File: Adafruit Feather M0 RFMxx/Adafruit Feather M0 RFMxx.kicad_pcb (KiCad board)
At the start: 2 copper layers, 50.8 x 22.9 mm, 41 parts, among them SW1 SPST_TACT-KMR2, U1 2MB Flash, U2 AP2112K-3.3, U3 MCP73831T-2ACI/OT, U4 RFM69HCW, X1 JSTPH, X2 32.768, X3 microUSB, X4 uFL

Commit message: This is version 0.1 of qwiic and flash board.
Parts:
- added U$31: MOUNTINGHOLE2.5, Adafruit Feather M0 RFMxx:MOUNTINGHOLE_2.5_PLATED, F.Cu at (141.6, 119.2)
- added U$31: MOUNTINGHOLE2.5, Adafruit Feather M0 RFMxx:MOUNTINGHOLE_2.5_PLATED, F.Cu at (171.4, 96.1)
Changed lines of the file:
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@@
     (tracks 871)
     (zones 0)
-    (modules 41)
+    (modules 43)
     (nets 58)
   )
   (page A4)
   (layers
-    (0 Top signal hide)
-    (31 Bottom signal)
+    (0 Top signal)
+    (31 Bottom signal hide)
     (32 B.Adhes user hide)
     (33 F.Adhes user hide)
     (34 B.Paste user hide)
     (35 F.Paste user hide)
-    (36 B.SilkS user)
+    (36 B.SilkS user hide)
     (37 F.SilkS user hide)
     (38 B.Mask user hide)
     (39 F.Mask user hide)
-    (40 Dwgs.User user)
+    (40 Dwgs.User user hide)
     (41 Cmts.User user hide)
     (42 Eco1.User user hide)
@@
     (mod_text_size 1 1)
     (mod_text_width 0.15)
-    (pad_size 1.524 1.524)
-    (pad_drill 0.762)
+    (pad_size 2.5 2.5)
+    (pad_drill 2.5)
     (pad_to_mask_clearance 0.051)
     (solder_mask_min_width 0.25)
@@
     (add_net VBUS)
   )
+  (module "Adafruit Feather M0 RFMxx:MOUNTINGHOLE_2.5_PLATED" (layer Top)
+    (at 141.6431 119.2276 270)
+    (fp_text reference U$31 (at 0 0 270) (layer F.SilkS) hide
+      (effects (font (size 1.27 1.27) (thickness 0.15)) (justify right top))
+    )
+    (fp_text value MOUNTINGHOLE2.5 (at 0 0 270) (layer F.SilkS) hide
+      (effects (font (size 1.27 1.27) (thickness 0.15)) (justify right top))
+    )
+    (fp_circle (center 0 0) (end 2 0) (layer F.SilkS) (width 0.2032))
+    (fp_circle (center 0 0) (end 1 0) (layer Dwgs.User) (width 2.032))
+    (fp_circle (center 0 0) (end 1 0) (layer Dwgs.User) (width 2.032))
+    (fp_circle (center 0 0) (end 1 0) (layer Dwgs.User) (width 2.032))
+    (fp_circle (center 0 0) (end 1 0) (layer Dwgs.User) (width 2.032))
+    (pad "" np_thru_hole circle (at -5.334 -29.718 270) (size 2.5 2.5) (drill 2.5) (layers *.Cu *.Mask)
+      (solder_mask_margin 0.0508))
+  )
+  (module "Adafruit Feather M0 RFMxx:MOUNTINGHOLE_2.5_PLATED" (layer Top)
+    (at 171.45 96.139 270)
+    (fp_text reference U$31 (at 0 0 270) (layer F.SilkS) hide
+      (effects (font (size 1.27 1.27) (thickness 0.15)) (justify right top))
+    )
+    (fp_text value MOUNTINGHOLE2.5 (at 0 0 270) (layer F.SilkS) hide
+      (effects (font (size 1.27 1.27) (thickness 0.15)) (justify right top))
+    )
+    (fp_circle (center 0 0) (end 2 0) (layer F.SilkS) (width 0.2032))
+    (fp_circle (center 0 0) (end 1 0) (layer Dwgs.User) (width 2.032))
+    (fp_circle (center 0 0) (end 1 0) (layer Dwgs.User) (width 2.032))
+    (fp_circle (center 0 0) (end 1 0) (layer Dwgs.User) (width 2.032))
+    (fp_circle (center 0 0) (end 1 0) (layer Dwgs.User) (width 2.032))
+    (pad "" np_thru_hole circle (at -0.0254 0.0889 270) (size 2.5 2.5) (drill 2.5) (layers *.Cu *.Mask)
+      (solder_mask_margin 0.0508))
+  )
   (module "Adafruit Feather M0 RFMxx:0805-NO" (layer Top)

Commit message: Parts mostly added. Need to confirm footprints. Before eliminating RFM parts.
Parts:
- added C31: 0.1uF, Adafruit Feather M0 RFMxx:0603-NO, F.Cu at (162.0, 85.8)
- added C32: 0.1uF, Adafruit Feather M0 RFMxx:0603-NO, F.Cu at (162.0, 87.3)
- added C33: 0.1uF, Adafruit Feather M0 RFMxx:0603-NO, F.Cu at (165.0, 85.8)
- added C35, C36: 22pF, Adafruit Feather M0 RFMxx:0603-NO, F.Cu at (148.5, 126.5)
- added J31: Conn_01x02, Socket_Strips:Socket_Strip_Straight_1x02_Pitch2.54mm, F.Cu at (175.8, 82.5)
- added J32: Conn_01x02, Pin_Headers:Pin_Header_Straight_1x02_Pitch2.54mm, F.Cu at (178.7, 88.0)
- added J33: Conn_01x02, Pin_Headers:Pin_Header_Straight_1x02_Pitch2.54mm, F.Cu at (197.7, 90.9)
- added R31: 60, Adafruit Feather M0 RFMxx:0603-NO, F.Cu at (176.7, 102.7)
- added R32: 60, Adafruit Feather M0 RFMxx:0603-NO, F.Cu at (176.7, 108.2)
- added U31: MCP25625-x-SS, Housings_SSOP:SSOP-28_5.3x10.2mm_Pitch0.65mm, F.Cu at (162.0, 106.4)
- added X31: XTAL-3.2X1.5, Adafruit Feather M0 RFMxx:XTAL3215, F.Cu at (185.4, 85.8)
- JP7: footprint SM04B-SRSS-TB(LFSN) -> SM04B-SRSS-TB(LF)(SN):SM04B-SRSS-TB(LFSN)
- moved U4 25.2 mm to (187.4, 104.7)
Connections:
- U4 pad 14P: /TXD_RST -> Net-(U4-Pad14P)
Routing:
- net Net-(U31-Pad20): vias 0 -> 1
- net GND: vias 32 -> 31

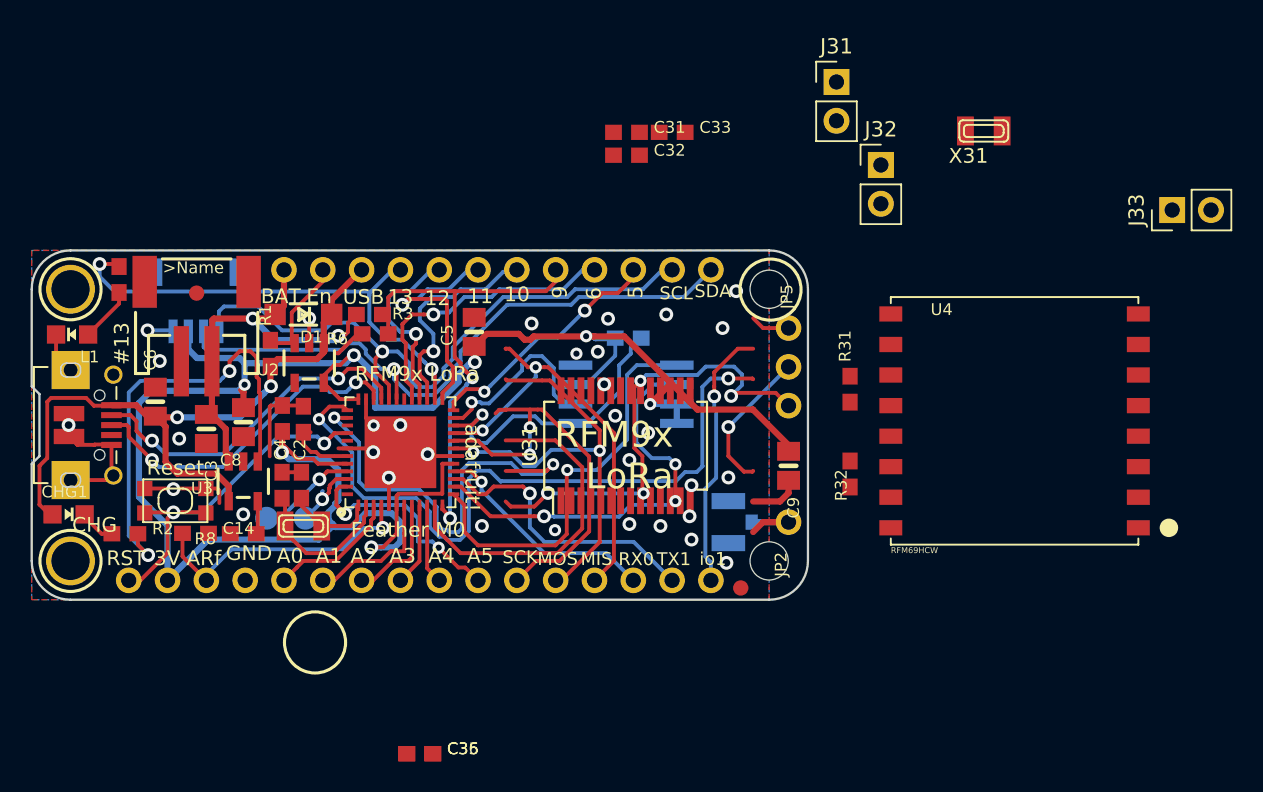
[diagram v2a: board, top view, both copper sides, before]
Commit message: Eliminated RFM and associated parts. Started to place and route. Must still confirm footprints.
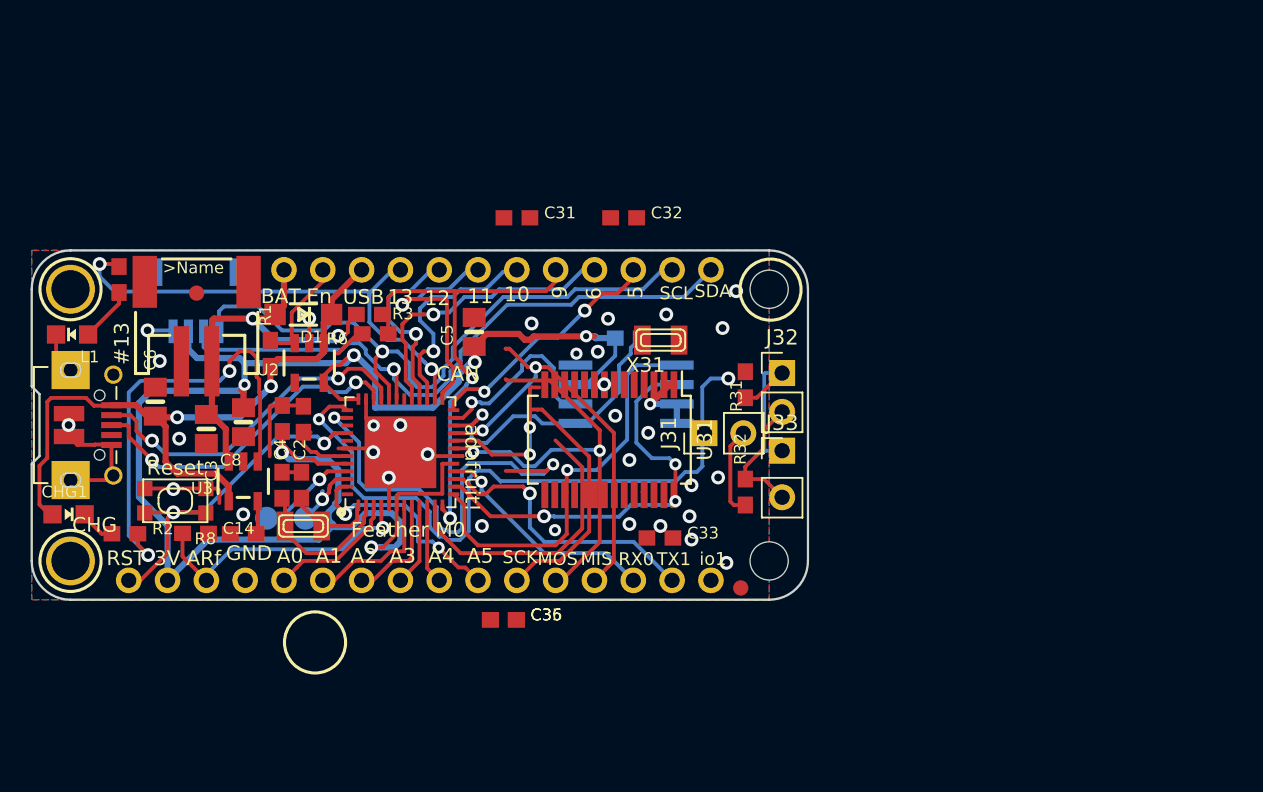
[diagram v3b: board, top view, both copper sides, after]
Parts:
- removed C9: 10uF, Adafruit Feather M0 RFMxx:0805-NO
- removed JP2: HEADER-1X1ROUND, Adafruit Feather M0 RFMxx:1X01_ROUND
- removed JP5: HEADER-1X3ROUND, Adafruit Feather M0 RFMxx:1X03_ROUND
- removed U4: RFM69HCW, Adafruit Feather M0 RFMxx:RFMHCW_SMT
- removed X4: uFL, Adafruit Feather M0 RFMxx:U.FL
- moved J33 30.3 mm to (172.2, 107.2), turned to 0 degrees
- moved C33 26.6 mm to (164.2, 112.4)
- moved X31 25.2 mm to (164.3, 99.4)
- moved J31 24.6 mm to (167.1, 105.5), turned to 90 degrees
- moved J32 15.1 mm to (172.2, 101.6)
- moved C35 10.3 mm to (154.0, 117.7)
- moved C36 10.3 mm to (154.0, 117.7)
- moved C31 9.10 mm to (154.9, 91.4)
- moved R32 6.96 mm to (169.8, 109.4), turned to 90 degrees
- moved R31 6.86 mm to (169.8, 102.4), turned to 270 degrees
- moved C32 4.10 mm to (161.8, 91.4)
- moved U31 1.13 mm to (160.9, 106.0), turned to 270 degrees
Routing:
- net /DIO5: track 30.5 -> 0.00 mm, vias 4 -> 0
- net /DIO1: track 17.3 -> 0.00 mm, vias 1 -> 0
- net +3V3: track 137.8 -> 121.7 mm
- net Net-(J32-Pad1): track 0.00 -> 10.4 mm
- net /DIO3: track 9.54 -> 0.00 mm, vias 1 -> 0
- net Net-(J32-Pad2): track 0.00 -> 8.30 mm
- net Net-(J31-Pad2): track 0.00 -> 5.90 mm
- net Net-(JP2-Pad1): track 5.00 -> 0.00 mm
- net GND: track 50.8 -> 47.1 mm
- net /D8_CS: track 22.2 -> 19.0 mm
- net /DIO2: track 2.58 -> 0.00 mm
- net /RXD_IRQ: track 46.0 -> 44.4 mm
- net Net-(U31-Pad20): vias 1 -> 0
- net Net-(C35-Pad1): vias 0 -> 1
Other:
- board text added: "CAN"
- board text removed: "RFM9x LoRa"

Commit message: Routing ...
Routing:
- net VBUS: track 44.9 -> 67.6 mm, vias 2 -> 3
- net /RXD_IRQ: track 44.4 -> 22.6 mm, vias 2 -> 1
- net /MOSI: track 29.3 -> 20.4 mm
- net /D8_CS: track 19.0 -> 10.2 mm
- net /TXD_RST: track 28.4 -> 25.1 mm
- net /MISO: track 27.1 -> 24.6 mm

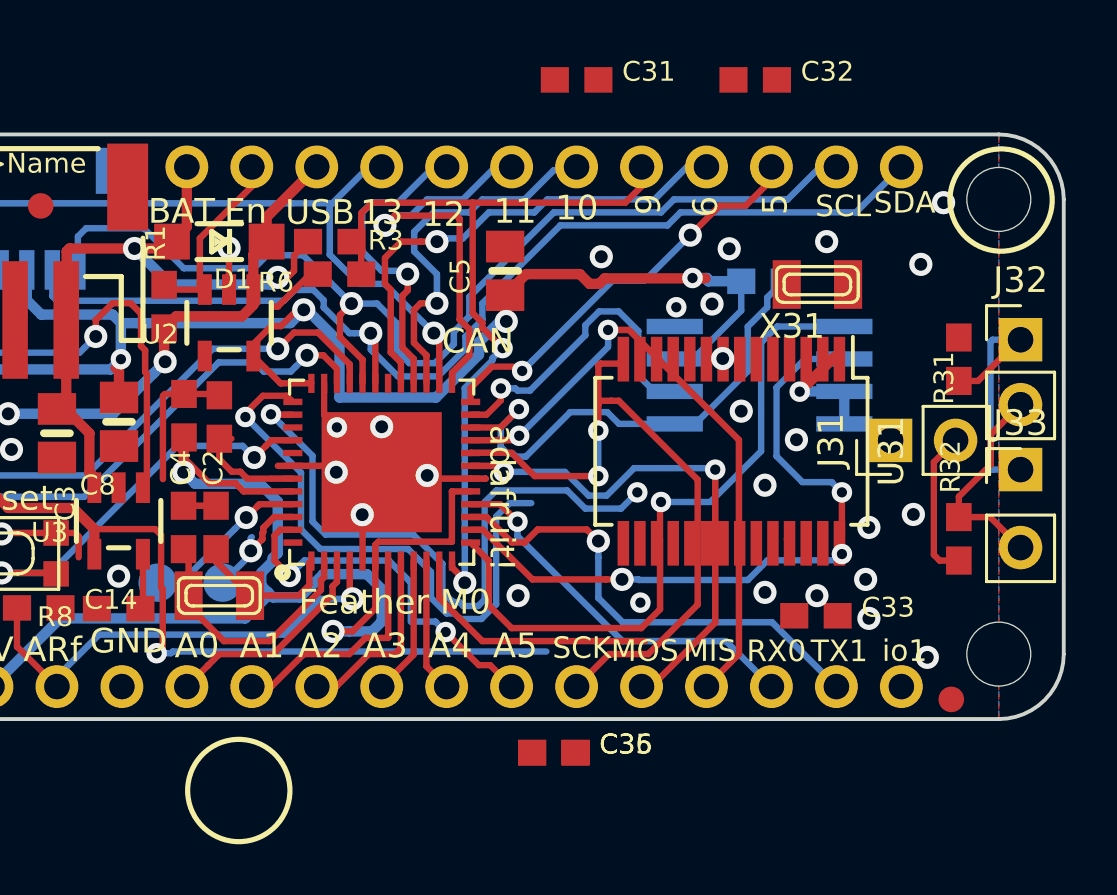
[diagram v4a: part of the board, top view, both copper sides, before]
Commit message: Routed, with some remaining errors: - some grounds disconnected - odd error about runner on PAD25 of MCP too close to PAD24. But there is no runner on PAD25 - just the footprint itself.
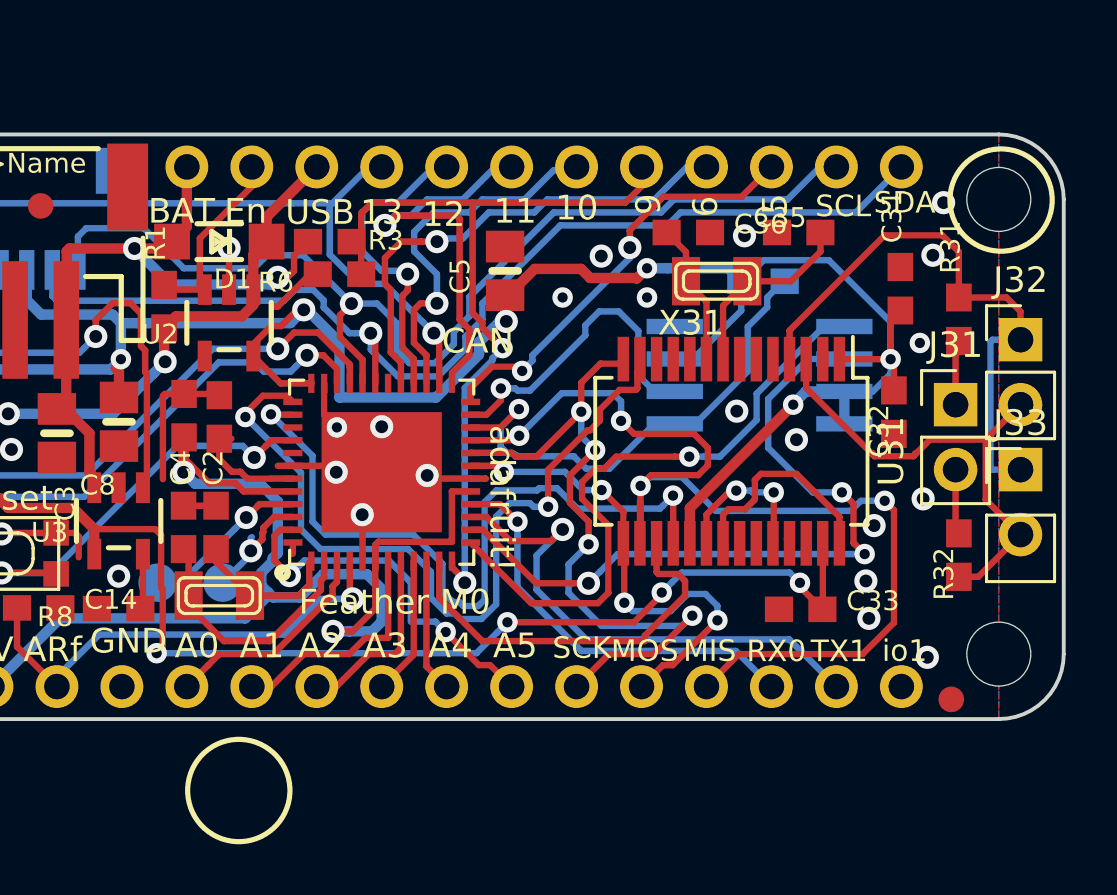
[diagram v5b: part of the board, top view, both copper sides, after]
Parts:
- J31: footprint Socket_Strips:Socket_Strip_Straight_1x02_Pitch2.54mm -> Pin_Headers:Pin_Header_Straight_1x02_Pitch2.54mm
- moved C35 22.5 mm to (163.5, 97.4), turned to 180 degrees
- moved C36 21.0 mm to (159.2, 97.4)
- moved C31 15.1 mm to (167.5, 99.6), turned to 90 degrees
- moved C32 14.1 mm to (167.3, 104.4), turned to 270 degrees
- moved X31 3.94 mm to (160.3, 99.3)
- moved J31 2.90 mm to (169.7, 104.1), turned to 0 degrees
- moved R31 1.56 mm to (169.8, 100.8), turned to 90 degrees
- moved C33 0.65 mm to (163.6, 112.1)
- moved R32 0.64 mm to (169.8, 110.0), turned to 270 degrees
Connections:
- net Net-(U$4-Pad39) renamed /TXLED
- net Net-(U$4-Pad41) renamed /USBHOSTEN
- net Net-(U$4-Pad48) renamed /RXLED
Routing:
- net +3V3: track 121.7 -> 143.6 mm, vias 7 -> 8
- net /MISO: track 24.6 -> 42.6 mm, vias 2 -> 4
- net VBUS: track 67.6 -> 83.2 mm, vias 3 -> 6
- net Net-(J32-Pad1): track 10.4 -> 22.5 mm
- net Net-(J32-Pad2): track 8.30 -> 18.9 mm
- net Net-(U31-Pad21): track 0.00 -> 8.52 mm
- net /RXD_IRQ: track 22.6 -> 31.0 mm, vias 1 -> 2
- net Net-(C35-Pad1): track 0.00 -> 7.53 mm, vias 1 -> 0
- net Net-(U31-Pad20): track 0.00 -> 6.18 mm, vias 0 -> 2
- net Net-(C36-Pad1): track 0.00 -> 5.60 mm
- net /D8_CS: track 10.2 -> 15.6 mm
- net Net-(J31-Pad2): track 5.90 -> 2.54 mm
- net /TXD_RST: track 25.1 -> 28.4 mm
- net /D4_FLASHMOSI: track 27.6 -> 24.7 mm
- net Net-(J31-Pad1): track 0.00 -> 2.54 mm
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
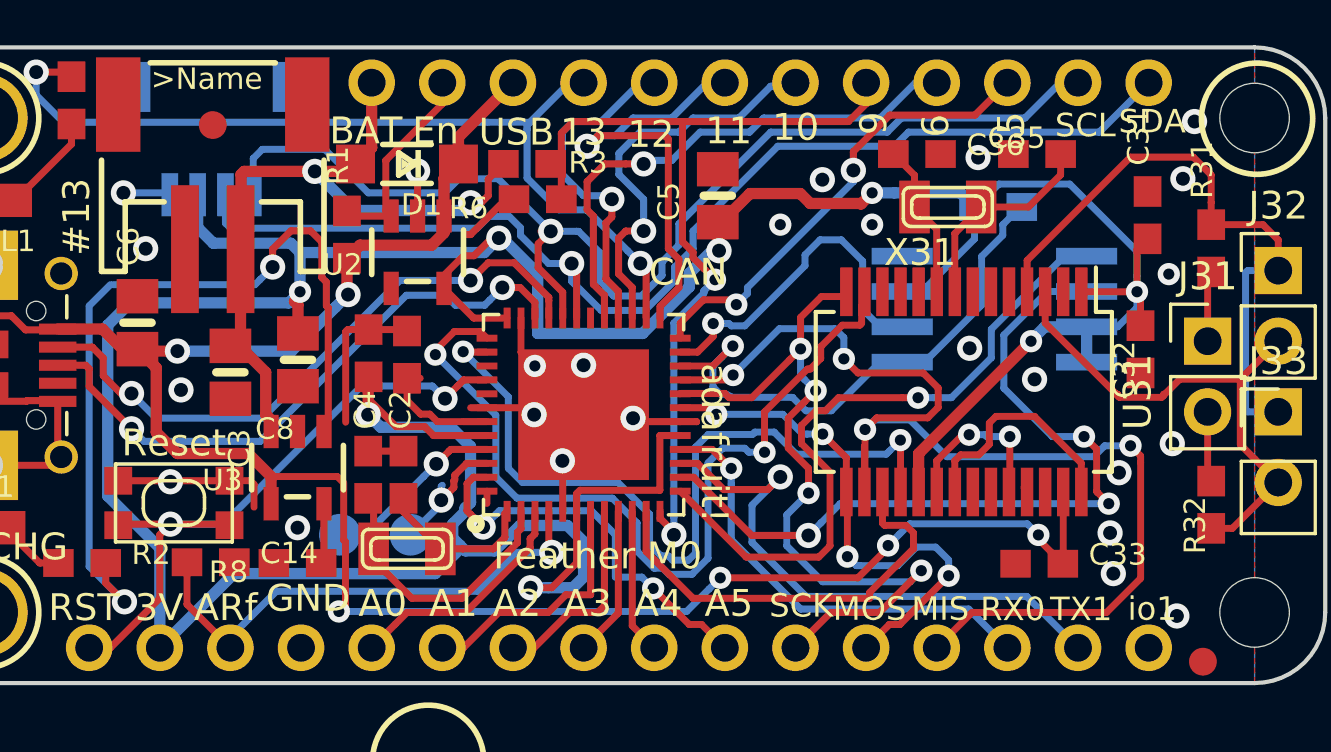
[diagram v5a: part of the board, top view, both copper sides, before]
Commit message: Fixed DRC errors. Remaining are ignores? - 2 pads part of USB connector - Top and Bottom regions not connected
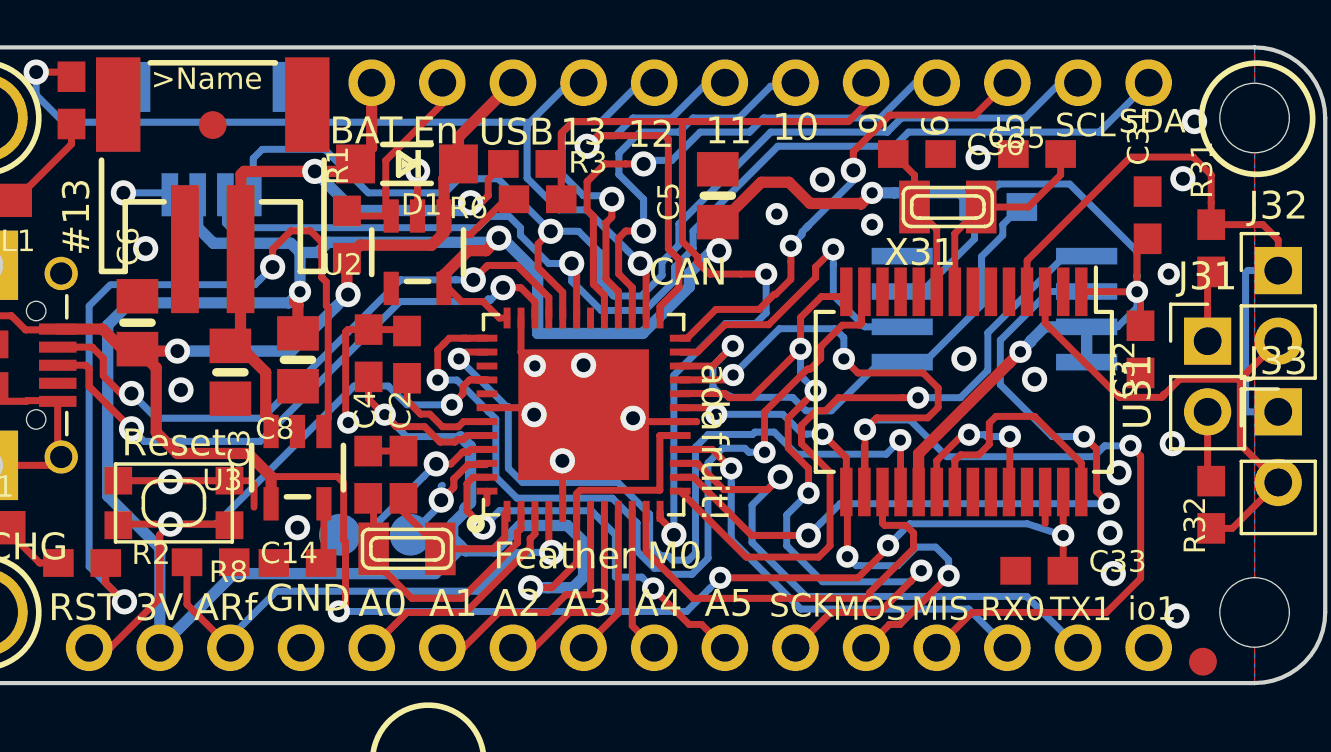
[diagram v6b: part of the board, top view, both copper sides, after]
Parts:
- moved C33 0.25 mm to (163.6, 112.4)
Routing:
- net /D9: track 31.9 -> 35.3 mm
- net +3V3: track 143.6 -> 141.1 mm
- net /~RESET: track 24.2 -> 25.0 mm
- net GND: track 47.1 -> 47.7 mm, vias 26 -> 27

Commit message: On MCP25625, added connection from STBY to GND to put device in Normal mode.
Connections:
- U31 pad 5: Net-(U31-Pad5) -> GND
